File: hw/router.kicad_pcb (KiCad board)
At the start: 2 copper layers, 83 x 43 mm, 59 parts, among them J1 USB_B, J2 SMA, J3 UART_01X03, J4 SWD_01X04, U1 MCP1826S, U2 USBLC6-2SC6, U3 HM-TRP-869S, U4 CP2102, U5 STM32F405RGTx, Y1 ABM7-8.000MHZ-D2Y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

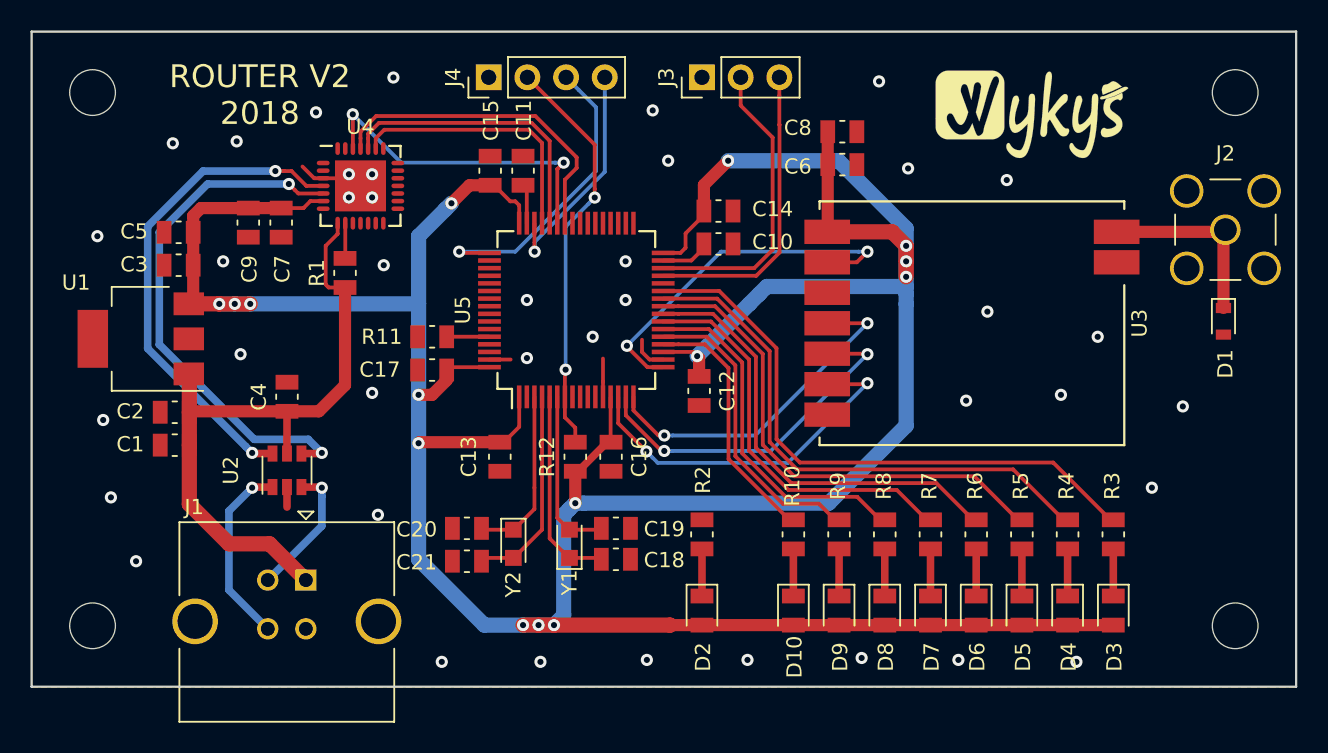
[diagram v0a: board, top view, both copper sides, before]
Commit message: added meanders
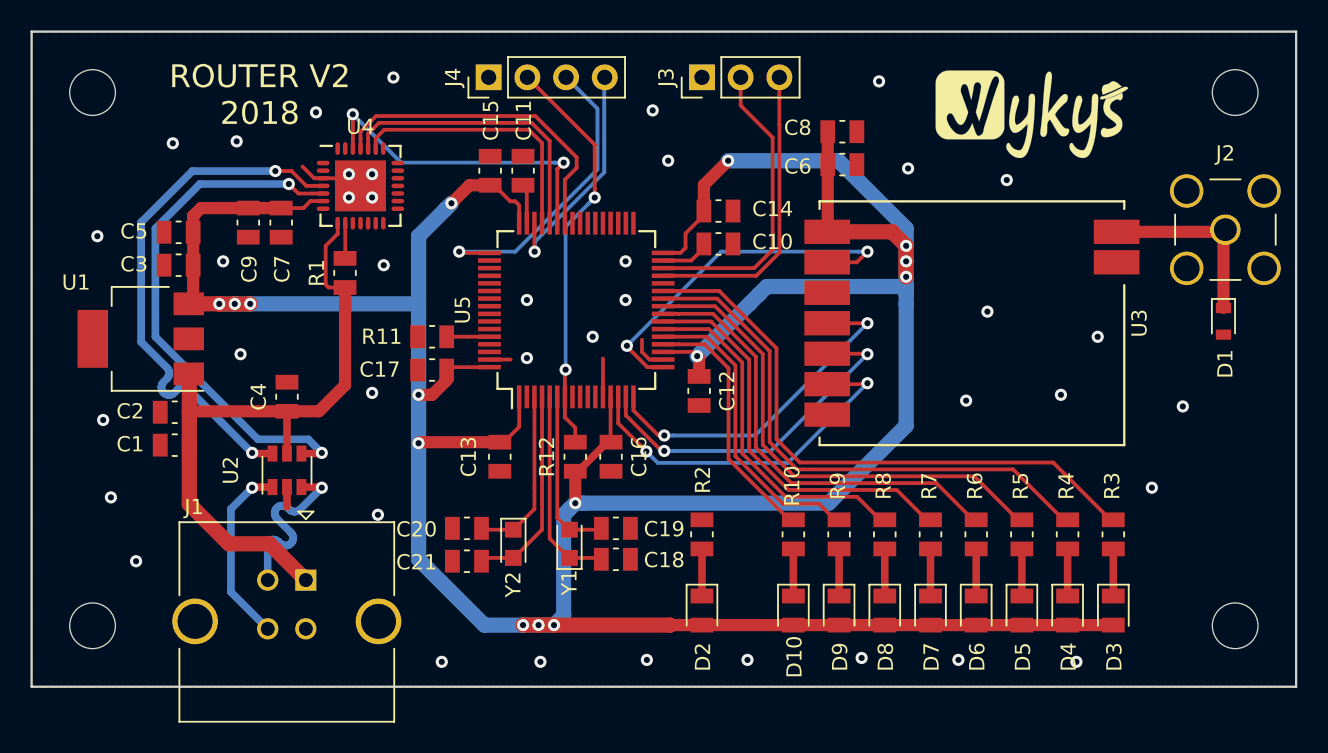
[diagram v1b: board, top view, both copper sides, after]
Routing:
- net /USB-: track 8.89 -> 12.2 mm
- net /D+: track 32.5 -> 35.0 mm

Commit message: added fiducials
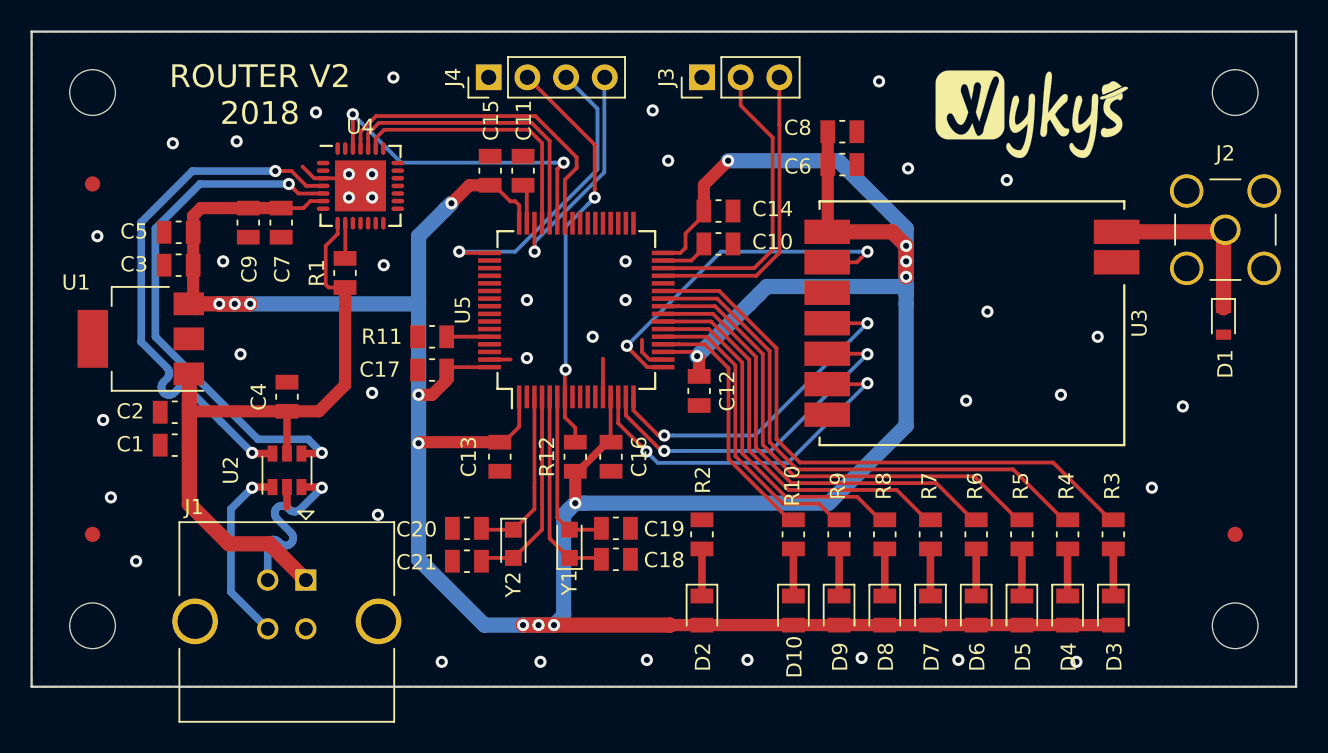
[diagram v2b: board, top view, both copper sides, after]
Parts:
- added REF**: Fiducial_Pad_1mm_Outer_2mm, KLIB_Mechanical:Fiducial_Pad_1mm_Outer_2mm, F.Cu at (190.0, 134.0)
- added REF**: Fiducial_Pad_1mm_Outer_2mm, KLIB_Mechanical:Fiducial_Pad_1mm_Outer_2mm, F.Cu at (115.0, 134.0)
- added REF**: Fiducial_Pad_1mm_Outer_2mm, KLIB_Mechanical:Fiducial_Pad_1mm_Outer_2mm, F.Cu at (115.0, 111.0)
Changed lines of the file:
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@@
     (tracks 513)
     (zones 0)
-    (modules 59)
+    (modules 62)
     (nets 93)
   )
@@
   )
   (setup
-    (last_trace_width 0.25)
+    (last_trace_width 1)
     (user_trace_width 0.5)
     (user_trace_width 0.8)
@@
       (xy 0.00501 -1.343155) (xy 0.015906 -1.34302)) (layer F.SilkS) (width 0.01))
   )
+  (module KLIB_Mechanical:Fiducial_Pad_1mm_Outer_2mm (layer F.Cu)
+    (at 190 134)
+    (descr "Circular Fiducial, 0.5mm bare copper top; 1mm keepout (Level C)")
+    (tags marker)
+    (attr virtual)
+    (fp_text reference REF** (at 0 -1.5) (layer F.SilkS) hide
+      (effects (font (size 1 1) (thickness 0.15)))
+    )
+    (fp_text value Fiducial_Pad_1mm_Outer_2mm (at 0 1.5) (layer F.Fab)
+      (effects (font (size 1 1) (thickness 0.15)))
+    )
+    (fp_circle (center 0 0) (end 0.75 0) (layer F.CrtYd) (width 0.05))
+    (fp_text user %R (at 0 0) (layer F.Fab)
+      (effects (font (size 0.2 0.2) (thickness 0.04)))
+    )
+    (fp_circle (center 0 0) (end 0.5 0) (layer F.Fab) (width 0.1))
+    (pad ~ smd circle (at 0 0) (size 1 1) (layers F.Cu F.Mask)
+      (solder_mask_margin 0.5) (clearance 0.5))
+  )
+  (module KLIB_Mechanical:Fiducial_Pad_1mm_Outer_2mm (layer F.Cu)
+    (at 115 134)
+    (descr "Circular Fiducial, 0.5mm bare copper top; 1mm keepout (Level C)")
+    (tags marker)
+    (attr virtual)
+    (fp_text reference REF** (at 0 -1.5) (layer F.SilkS) hide
+      (effects (font (size 1 1) (thickness 0.15)))
+    )
+    (fp_text value Fiducial_Pad_1mm_Outer_2mm (at 0 1.5) (layer F.Fab)
+      (effects (font (size 1 1) (thickness 0.15)))
+    )
+    (fp_circle (center 0 0) (end 0.75 0) (layer F.CrtYd) (width 0.05))
+    (fp_text user %R (at 0 0) (layer F.Fab)
+      (effects (font (size 0.2 0.2) (thickness 0.04)))
+    )
+    (fp_circle (center 0 0) (end 0.5 0) (layer F.Fab) (width 0.1))
+    (pad ~ smd circle (at 0 0) (size 1 1) (layers F.Cu F.Mask)
+      (solder_mask_margin 0.5) (clearance 0.5))
+  )
+  (module KLIB_Mechanical:Fiducial_Pad_1mm_Outer_2mm (layer F.Cu)
+    (at 115 111)
+    (descr "Circular Fiducial, 0.5mm bare copper top; 1mm keepout (Level C)")
+    (tags marker)
+    (attr virtual)
+    (fp_text reference REF** (at 0 -1.5) (layer F.SilkS) hide
+      (effects (font (size 1 1) (thickness 0.15)))
+    )
+    (fp_text value Fiducial_Pad_1mm_Outer_2mm (at 0 1.5) (layer F.Fab)
+      (effects (font (size 1 1) (thickness 0.15)))
+    )
+    (fp_circle (center 0 0) (end 0.75 0) (layer F.CrtYd) (width 0.05))
+    (fp_text user %R (at 0 0) (layer F.Fab)
+      (effects (font (size 0.2 0.2) (thickness 0.04)))
+    )
+    (fp_circle (center 0 0) (end 0.5 0) (layer F.Fab) (width 0.1))
+    (pad ~ smd circle (at 0 0) (size 1 1) (layers F.Cu F.Mask)
+      (solder_mask_margin 0.5) (clearance 0.5))
+  )
   (gr_text "ROUTER V2\n2018" (at 125.984 105.156) (layer F.SilkS)
     (effects (font (size 1.5 1.5) (thickness 0.3)))
@@
   (segment (start 139.147161 115.525161) (end 139.065 115.443) (width 0.25) (layer F.Cu) (net 56))
   (segment (start 141.053629 115.525161) (end 139.147161 115.525161) (width 0.25) (layer F.Cu) (net 56))
-  (segment (start 189.23 119.14) (end 189.23 114.127) (width 0.8) (layer F.Cu) (net 70))
-  (segment (start 189.23 114.127) (end 189.357 114) (width 0.8) (layer F.Cu) (net 70))
-  (segment (start 182.22 114.142) (end 189.215 114.142) (width 0.8) (layer F.Cu) (net 70))
-  (segment (start 189.215 114.142) (end 189.357 114) (width 0.8) (layer F.Cu) (net 70))
+  (segment (start 189.23 119.14) (end 189.23 114.127) (width 1) (layer F.Cu) (net 70))
+  (segment (start 189.23 114.127) (end 189.357 114) (width 1) (layer F.Cu) (net 70))
+  (segment (start 182.22 114.142) (end 189.215 114.142) (width 1) (layer F.Cu) (net 70))
+  (segment (start 189.215 114.142) (end 189.357 114) (width 1) (layer F.Cu) (net 70))
   (segment (start 144.003629 132.337371) (end 144.003629 130.940371) (width 0.25) (layer F.Cu) (net 89))
   (segment (start 142.621 133.695) (end 140.619 133.695) (width 0.25) (layer F.Cu) (net 89))
